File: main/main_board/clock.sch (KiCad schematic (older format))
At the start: 11 parts, among them J2 MCLK, U10 74AUP1G74, U12 FIN1047, X2 570CAC000121DG

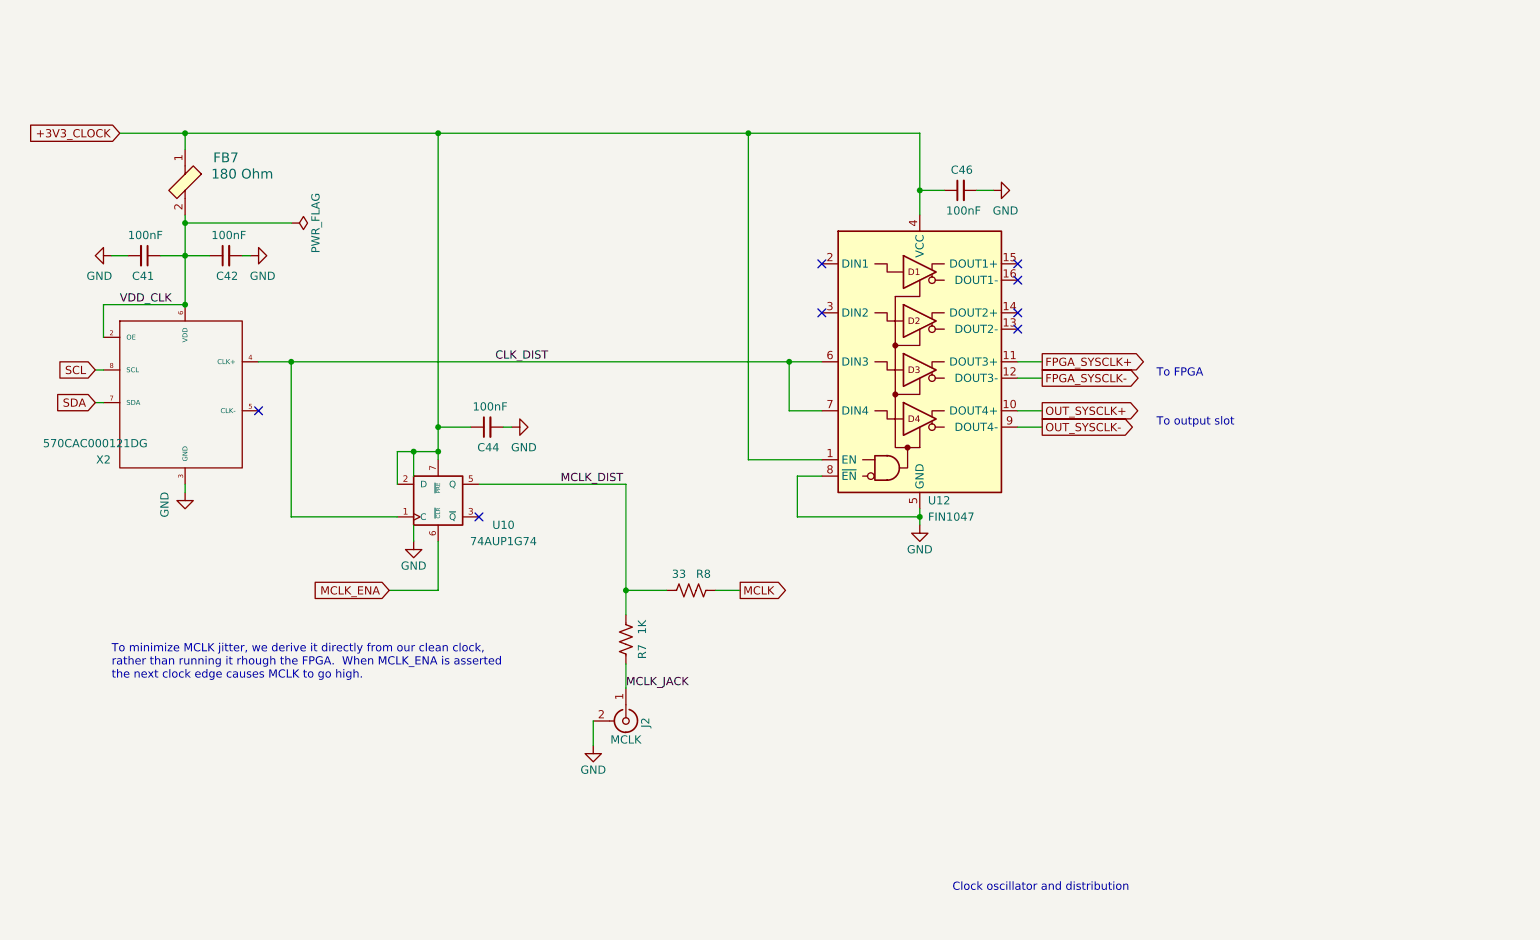
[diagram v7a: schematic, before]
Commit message: Added testpoints, debug IO port, LEDs, and clock output jack.
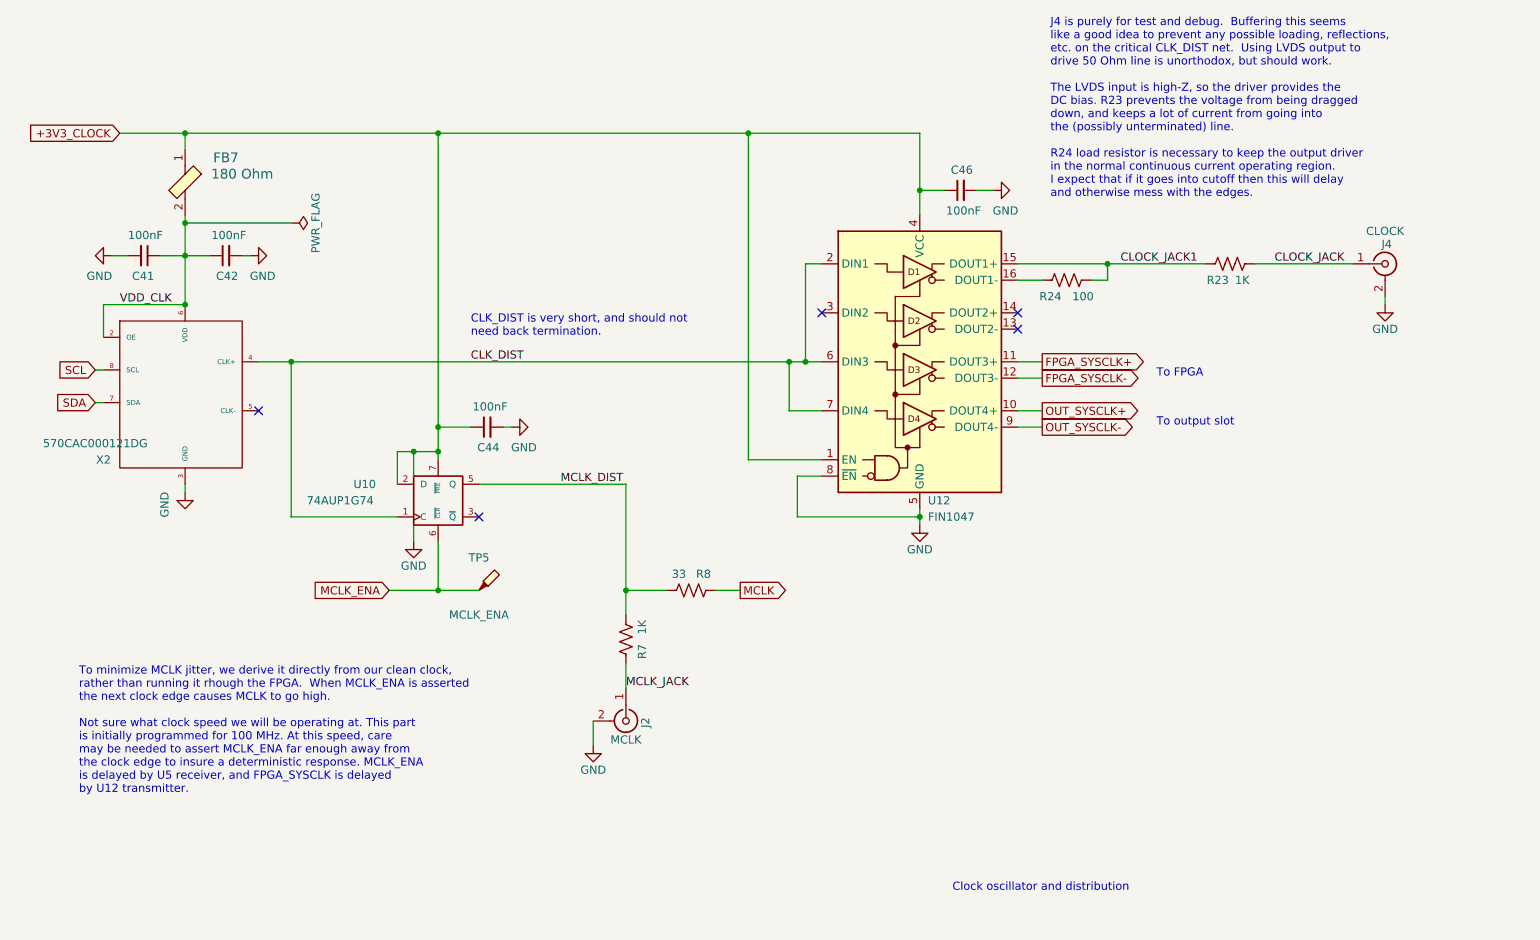
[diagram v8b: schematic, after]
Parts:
- added J4: CLOCK, Connector_Coaxial:MMCX_Molex_73415-1471_Vertical, symbol Connector:Conn_Coaxial
- added R23: 1K, Resistor_SMD:R_0603_1608Metric, symbol Device:R_US
- added R24: 100, Resistor_SMD:R_0603_1608Metric, symbol Device:R_US
- added TP5: MCLK_ENA, TestPoint:TestPoint_Pad_D1.0mm, symbol Connector:TestPoint_Probe
- J2: DK line (none) -> 35
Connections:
- net CLK_DIST: now also U12.2 (DIN1)
- net GND: now also J4.2 (Ext)
- net MCLK_ENA: now also TP5.1
- net CLOCK_JACK1: now reaches U12.15 (DOUT1+)
- net CLOCK_JACK1: now also R23.2, R24.2
- net at U12.16 (DOUT1-): now also R24.1
- new net CLOCK_JACK: J4.1 (In), R23.1
- no-connect marks 8 -> 5
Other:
- note added: "CLK_DIST is very short, and should not\nneed back termination."
- note added: "J4 is purely for test and debug. Buffering this seems\nlike a good idea to prevent any possible loading, reflections,\netc. on the critical CLK_DIST net. Using LVDS output to \ndrive 50 Ohm line is unorthodox, but should work. \n\nThe LVDS input is high-Z, so the driver provides the\nDC bias. R23 prevents the voltage from being dragged\ndown, and keeps a lot of current from going into\nthe (possi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"
- note added: "To minimize MCLK jitter, we derive it directly from our clean clock, \nrather than running it rhough the FPGA. When MCLK_ENA is asserted\nthe next clock edge causes MCLK to go high. \n\nNot sure what clock speed we will be operating at. This part\nis initially programmed for 100 MHz. At this speed, care\nmay be needed to assert MCLK_ENA far enough away from \nthe clock edge to insure a determinis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"
- note removed: "To minimize MCLK jitter, we derive it directly from our clean clock, \nrather than running it rhough the FPGA. When MCLK_ENA is asserted\nthe next clock edge causes MCLK to go high."
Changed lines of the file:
@@
 U 1 1 5EBEEE85
 P 4450 4450
-F 0 "U10" H 4850 4300 50  0000 C CNN
-F 1 "74AUP1G74" H 4850 4200 50  0000 C CNN
+F 0 "U10" H 4000 4550 50  0000 C CNN
+F 1 "74AUP1G74" H 3850 4450 50  0000 C CNN
 F 2 "Package_SO:VSSOP-8_2.3x2mm_P0.5mm" H 4450 4450 50  0001 C CNN
 F 3 "https://assets.nexperia.com/documents/data-sheet/74AUP1G74.pdf" H 4450 4450 50  0001 C CNN
@@
 Text GLabel 4150 5000 0    50   Input ~ 0
 MCLK_ENA
-Text Notes 2450 5550 0    50   ~ 0
-To minimize MCLK jitter, we derive it directly from our clean clock, \nrather than running it rhough the FPGA.  When MCLK_ENA is asserted\nthe next clock edge causes MCLK to go high.
+Text Notes 2250 6250 0    50   ~ 0
+To minimize MCLK jitter, we derive it directly from our clean clock, \nrather than running it rhough the FPGA.  When MCLK_ENA is asserted\nthe next clock edge causes MCLK to go high.  \n\nNot sure what clock speed we will be operating at. This part\nis initially programmed for 100 MHz. At this speed, care\nmay be needed to assert MCLK_ENA far enough away from \nthe clock edge to insure a deterministic response. MCLK_ENA \nis delayed by U5 receiver, and FPGA_SYSCLK is delayed\nby U12 transmitter.
 Wire Wire Line
 	7400 4500 7400 4550
@@
 Connection ~ 6600 3600
 Wire Wire Line
-	6600 3600 6800 3600
+	6600 3600 6700 3600
 Text GLabel 8150 3600 2    50   Output ~ 0
 FPGA_SYSCLK+
@@
 $EndComp
 Wire Wire Line
-	7400 2200 6350 2200
-Wire Wire Line
 	2900 2200 2900 2300
 Wire Wire Line
@@
 F 2 "Connector_Coaxial:MMCX_Molex_73415-1471_Vertical" H 5600 5800 50  0001 C CNN
 F 3 "https://www.molex.com/pdm_docs/sd/734151471_sd.pdf" H 5600 5800 50  0001 C CNN
-F 4 "" H 5600 5800 50  0001 C CNN "DK line"
+F 4 "35" H 5600 5800 50  0001 C CNN "DK line"
 F 5 "CONN MMCX JACK STR 50 OHM PCB" H 5600 5800 50  0001 C CNN "Description"
 F 6 "WM5557-ND" H 5600 5800 50  0001 C CNN "Digikey"
@@
 NoConn ~ 8000 3400
 NoConn ~ 8000 3300
-NoConn ~ 8000 3100
-NoConn ~ 8000 3000
 Text Label 2500 3250 0    50   ~ 0
 VDD_CLK
-Text Label 4800 3600 0    50   ~ 0
+Text Label 4650 3600 0    50   ~ 0
 CLK_DIST
 Text Label 5200 4350 0    50   ~ 0
@@
 Wire Wire Line
 	6350 2200 4450 2200
-NoConn ~ 6800 3000
 NoConn ~ 6800 3300
+$Comp
+L Connector:TestPoint_Probe TP?
+U 1 1 5F1B0EE8
+P 4700 5000
+AR Path="/5DFCF14D/5DA78AA2/5F1B0EE8" Ref="TP?"  Part="1"
+AR Path="/5DFCF14D/5E295469/5F1B0EE8" Ref="TP?"  Part="1"
+AR Path="/5DFCF14D/5E195558/5F1B0EE8" Ref="TP?"  Part="1"
+AR Path="/5F1B0EE8" Ref="TP?"  Part="1"
+AR Path="/5E525FC9/5F1B0EE8" Ref="TP?"  Part="1"
+AR Path="/5E525F87/5F1B0EE8" Ref="TP?"  Part="1"
+AR Path="/5E525F2C/5F1B0EE8" Ref="TP5"  Part="1"
+F 0 "TP5" H 4700 5200 50  0000 C CNN
+F 1 "MCLK_ENA" H 4700 4850 50  0000 C CNN
+F 2 "TestPoint:TestPoint_Pad_D1.0mm" H 4900 5000 50  0001 C CNN
+F 3 "~" H 4900 5000 50  0001 C CNN
+F 4 "Do Not Populate" H 4700 5000 50  0001 C CNN "Description"
+F 5 "DNP" H 4700 5000 50  0001 C CNN "MPN"
+	1    4700 5000
+	1    0    0    -1
+$EndComp
+Wire Wire Line
+	4450 5000 4700 5000
+Connection ~ 4450 5000
+$Comp
+L Connector:Conn_Coaxial J4
+U 1 1 5F1FA525
+P 10250 3000
+AR Path="/5E525F2C/5F1FA525" Ref="J4"  Part="1"
+AR Path="/5E525FFE/5F1FA525" Ref="J?"  Part="1"
+F 0 "J4" H 10260 3120 50  0000 C CNN
+F 1 "CLOCK" H 10250 3200 50  0000 C CNN
+F 2 "Connector_Coaxial:MMCX_Molex_73415-1471_Vertical" H 10250 3000 50  0001 C CNN
+F 3 "https://www.molex.com/pdm_docs/sd/734151471_sd.pdf" H 10250 3000 50  0001 C CNN
+F 4 "35" H 10250 3000 50  0001 C CNN "DK line"
+F 5 "CONN MMCX JACK STR 50 OHM PCB" H 10250 3000 50  0001 C CNN "Description"
+F 6 "WM5557-ND" H 10250 3000 50  0001 C CNN "Digikey"
+F 7 "0734151471" H 10250 3000 50  0001 C CNN "MPN"
+F 8 "Molex" H 10250 3000 50  0001 C CNN "Manufacturer"
+	1    10250 3000
+	1    0    0    -1
+$EndComp
+$Comp
+L power:GND #PWR?
+U 1 1 5F1FA52B
+P 10250 3250
+AR Path="/5E624B3C/5F1FA52B" Ref="#PWR?"  Part="1"
+AR Path="/5E525F2C/5F1FA52B" Ref="#PWR0135"  Part="1"
+AR Path="/5E525FFE/5F1FA52B" Ref="#PWR?"  Part="1"
+F 0 "#PWR0135" H 10250 3000 50  0001 C CNN
+F 1 "GND" H 10250 3100 50  0000 C CNN
+F 2 "" H 10250 3250 50  0001 C CNN
+F 3 "" H 10250 3250 50  0001 C CNN
+	1    10250 3250
+	1    0    0    -1
+$EndComp
+Wire Wire Line
+	10250 3250 10250 3200
+Wire Wire Line
+	6800 3000 6700 3000
+Wire Wire Line
+	6700 3000 6700 3600
+Connection ~ 6700 3600
+Wire Wire Line
+	6700 3600 6800 3600
+Wire Wire Line
+	8000 3000 8550 3000
+Wire Wire Line
+	6350 2200 7400 2200
+Text Notes 8200 2600 0    50   ~ 0
+J4 is purely for test and debug.  Buffering this seems\nlike a good idea to prevent any possible loading, reflections,\netc. on the critical CLK_DIST net.  Using LVDS output to \ndrive 50 Ohm line is unorthodox, but should work.  \n\nThe LVDS input is high-Z, so the driver provides the\nDC bias. R23 prevents the voltage from being dragged\ndown, and keeps a lot of current from going into\nthe (possibly unterminated) line.\n\nR24 load resistor is necessary to keep the output driver \nin the normal continuous current operating region. \nI expect that if it goes into cutoff then this will delay \nand otherwise mess with the edges.
+$Comp
+L Device:R_US R?
+U 1 1 5F262166
+P 8300 3100
+AR Path="/5DFF6C0D/5F262166" Ref="R?"  Part="1"
+AR Path="/5E1D6729/5E1DA2AA/5F262166" Ref="R?"  Part="1"
+AR Path="/5E2EB92B/5F262166" Ref="R?"  Part="1"
+AR Path="/5E51E83D/5F262166" Ref="R?"  Part="1"
+AR Path="/5F262166" Ref="R?"  Part="1"
+AR Path="/5E525F2C/5F262166" Ref="R24"  Part="1"
+AR Path="/5E525F87/5F262166" Ref="R?"  Part="1"
+AR Path="/5E525FFE/5F262166" Ref="R?"  Part="1"
+F 0 "R24" V 8200 3200 50  0000 C CNN
+F 1 "100" V 8200 3000 50  0000 C CNN
+F 2 "Resistor_SMD:R_0603_1608Metric" V 8340 3090 50  0001 C CNN
+F 3 "https://www.seielect.com/catalog/sei-rncp.pdf" H 8300 3100 50  0001 C CNN
+F 4 "RNCP0603FTD100RCT-ND" H 8300 3100 50  0001 C CNN "Digikey"
+F 5 "29" H 8300 3100 50  0001 C CNN "DK line"
+F 6 "RES 100 OHM 1% 1/8W 0603" H 8300 3100 50  0001 C CNN "Description"
+F 7 "RNCP0603FTD100R" H 8300 3100 50  0001 C CNN "MPN"
+F 8 "Stackpole Electronics Inc" H 8300 3100 50  0001 C CNN "Manufacturer"
+	1    8300 3100
+	0    -1   -1   0
+$EndComp
+Wire Wire Line
+	8150 3100 8000 3100
+Wire Wire Line
+	8450 3100 8550 3100
+Wire Wire Line
+	8550 3100 8550 3000
+Connection ~ 8550 3000
+$Comp
+L Device:R_US R?
+U 1 1 5F268B4E
+P 9300 3000
+AR Path="/5DFF6C0D/5F268B4E" Ref="R?"  Part="1"
+AR Path="/5E1D6729/5E1DA2AA/5F268B4E" Ref="R?"  Part="1"
+AR Path="/5E2EB92B/5F268B4E" Ref="R?"  Part="1"
+AR Path="/5E51E83D/5F268B4E" Ref="R?"  Part="1"
+AR Path="/5F268B4E" Ref="R?"  Part="1"
+AR Path="/5E525F2C/5F268B4E" Ref="R23"  Part="1"
+AR Path="/5E525FFE/5F268B4E" Ref="R?"  Part="1"
+F 0 "R23" V 9400 2925 50  0000 C CNN
+F 1 "1K" V 9400 3075 50  0000 C CNN
+F 2 "Resistor_SMD:R_0603_1608Metric" V 9340 2990 50  0001 C CNN
+F 3 "https://www.seielect.com/catalog/sei-rncp.pdf" H 9300 3000 50  0001 C CNN
+F 4 "31" H 9300 3000 50  0001 C CNN "DK line"
+F 5 "RES 1K OHM 1% 1/8W 0603" H 9300 3000 50  0001 C CNN "Description"
+F 6 "RNCP0603FTD1K00CT-ND" H 9300 3000 50  0001 C CNN "Digikey"
+F 7 "RNCP0603FTD1K00" H 9300 3000 50  0001 C CNN "MPN"
+F 8 "Stackpole Electronics Inc" H 9300 3000 50  0001 C CNN "Manufacturer"
+	1    9300 3000
+	0    1    1    0
+$EndComp
+Wire Wire Line
+	8550 3000 9150 3000
+Text Notes 4650 3450 0    50   ~ 0
+CLK_DIST is very short, and should not\nneed back termination.
+Text Label 10000 3000 2    50   ~ 0
+CLOCK_JACK
+Wire Wire Line
+	9450 3000 10050 3000
+Text Label 9100 3000 2    50   ~ 0
+CLOCK_JACK1
 $EndSCHEMATC
